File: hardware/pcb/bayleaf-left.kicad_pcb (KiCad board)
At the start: 2 copper layers, 134.9 x 92.3 mm, 70 parts, among them SW1 PG1316S, SW10 PG1316S, SW11 PG1316S, SW12 PG1316S, SW13 PG1316S, SW14 PG1316S, SW15 PG1316S, SW16 PG1316S, SW17 PG1316S, SW18 PG1316S, SW19 PG1316S, SW2 PG1316S, SW20 PG1316S, SW21 PG1316S, SW22 PG1316S, SW23 PG1316S, SW24 PG1316S, SW25 PG1316S, SW26 PG1316S, SW27 PG1316S, SW28 PG1316S, SW29 PG1316S, SW3 PG1316S, SW30 PG1316S, SW31 KMR211NGLFS, SW4 PG1316S, SW5 PG1316S, SW6 PG1316S, SW7 PG1316S, SW8 PG1316S, SW9 PG1316S, U1 nice!nano v2

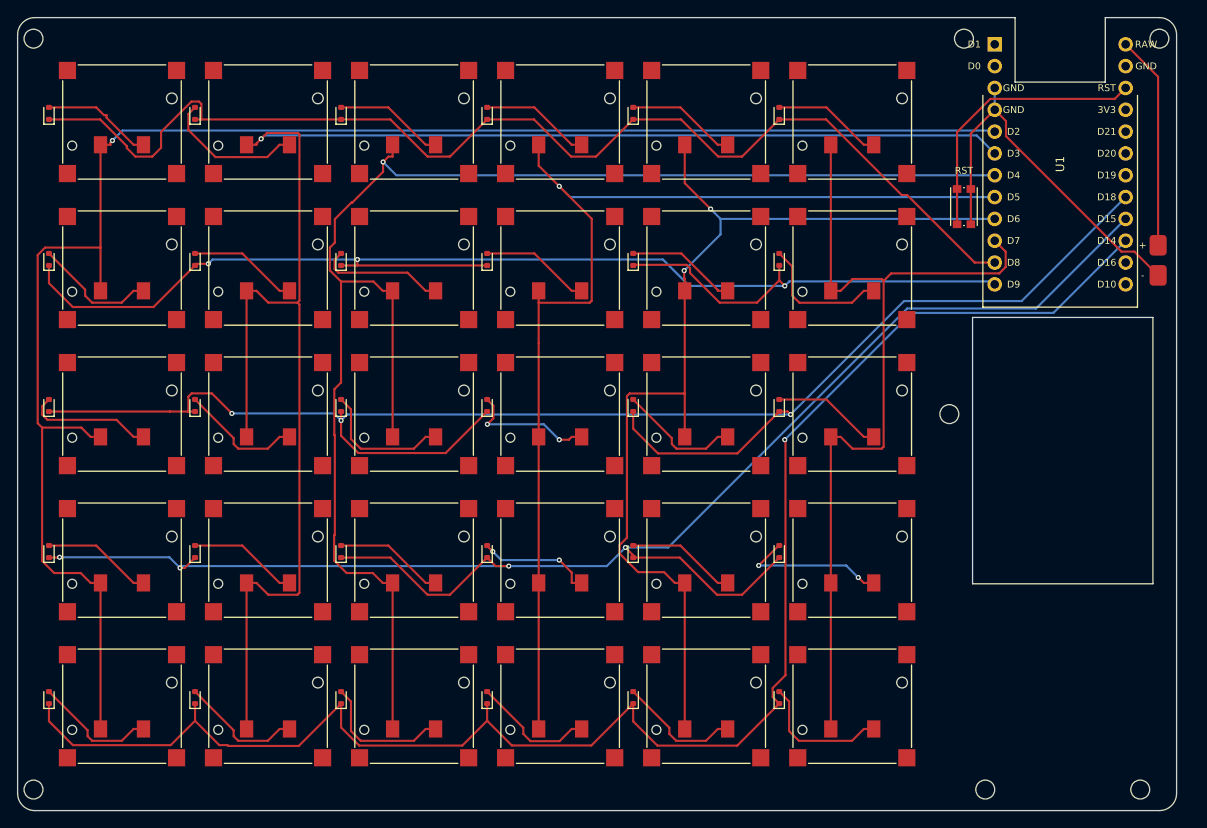
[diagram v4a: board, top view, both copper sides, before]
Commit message: Hand-solderable switches, FR4 bottom plate, reset button on the underside
- PCB: new Kailh_PG1316S_castellated footprint (window under each switch, contacts on plated
  half-holes, soldered from below with an iron; frame anchors on a small hotplate), after
  Mike Holscher's mikecinq, drawn from the Kailh land pattern. Order with castellated holes.
  Routing gets notched keepouts so Freerouting can reach the half-hole pads.
- Reset (KMR2) moves to the bottom side; the pin-hole in the plateau is gone.
- Bottom plate is now a copper-free 0.8 mm FR4 board (generate_pcb.py PlateBuilder, gerbers
  in fab/plate-*) so the radio isn't boxed in by aluminium; windows for the switch solder,
  nice!nano pins, reset button and USB-C.
- Renders (new underside view), BOM, ordering, assembly, case and schematic docs updated.

Co-Authored-By: Claude Opus 5.5 <noreply@anthropic.com>
Claude-Session: https://claude.ai/code/session_01C1HRLCKaYQawWFomwAvAgT
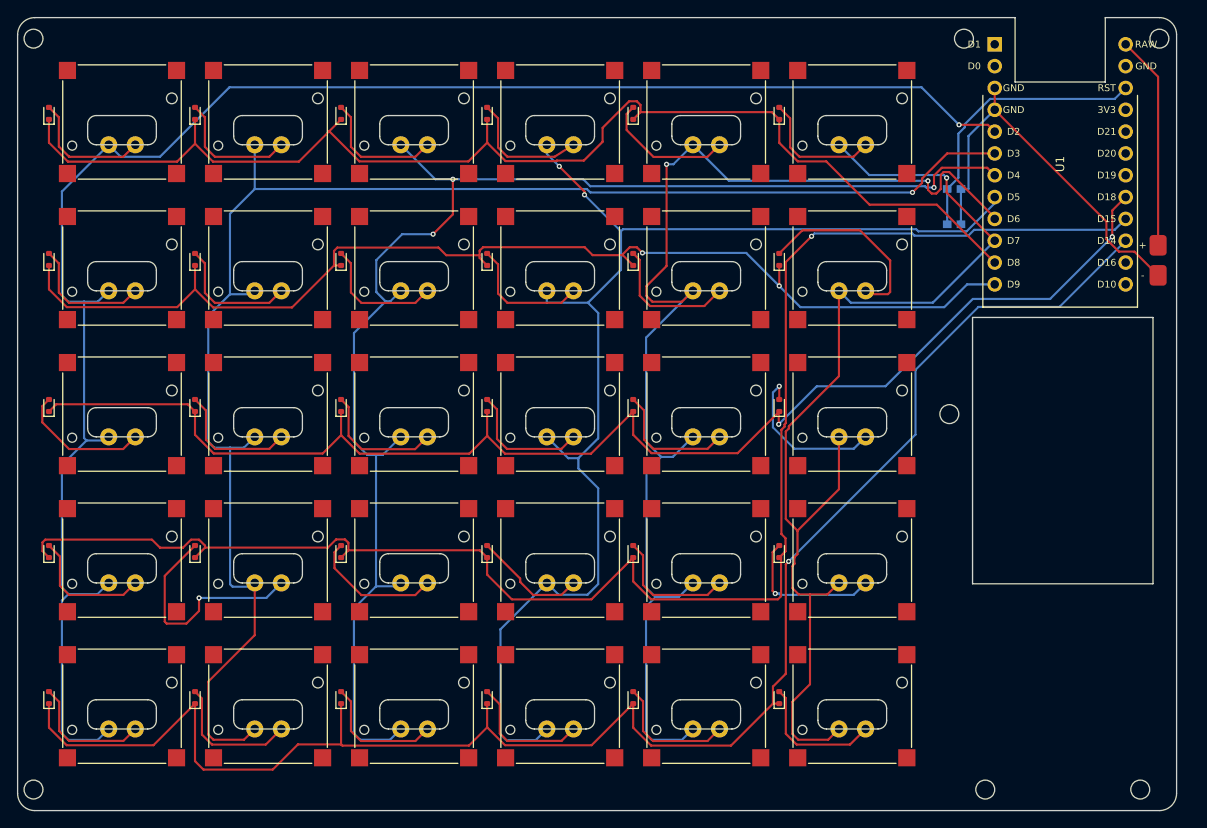
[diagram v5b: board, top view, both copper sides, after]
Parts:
- SW1, SW10, SW11, SW12, SW13, SW14, SW15, SW16, SW17, SW18, SW19, SW2, SW20, SW21, SW22, SW23, SW24, SW25, SW26, SW27, SW28, SW29, SW3, SW30, SW4, SW5, SW6, SW7, SW8, SW9: footprint bayleaf:Kailh_PG1316S -> bayleaf:Kailh_PG1316S_castellated
- SW31: moved to B.Cu
- moved SW31 1.15 mm to (109.0, 22.0), turned to -90 degrees
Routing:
- net ROW2: track 186.4 -> 160.7 mm, vias 3 -> 2
- net COL5: track 102.4 -> 125.9 mm, vias 0 -> 1
- net ROW1: track 157.8 -> 134.5 mm, vias 3 -> 2
- net COL4: track 120.9 -> 141.1 mm
- net COL3: track 129.2 -> 148.5 mm, vias 1 -> 2
- net COL1: track 194.2 -> 179.7 mm
- net N_SW20: track 12.8 -> 26.8 mm, vias 0 -> 1
- net COL2: track 172.9 -> 163.7 mm, vias 1 -> 3
- net ROW0: track 136.0 -> 142.5 mm
- net N_SW12: track 15.9 -> 22.3 mm
- net N_SW18: track 12.8 -> 19.0 mm, vias 0 -> 1
- net ROW3: track 190.6 -> 184.6 mm, vias 4 -> 1
- net COL0: track 197.6 -> 201.7 mm
- net N_SW11: track 12.9 -> 15.8 mm
- net N_SW21: track 12.8 -> 15.7 mm
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
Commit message: Switch frame anchors solderable from below: plated holes in the anchor pads
- Kailh_PG1316S_castellated: each 2x2 mm frame-anchor pad gets a 0.7 mm plated hole with a
  1.4 mm pad on the bottom, so the whole switch can be soldered from the underside with an
  iron (hotplate still works). Switch window narrowed to 7.2 mm to keep routing channels.
- Bottom plates: 2.6 mm windows under every anchor hole; silkscreen moved under the battery.
- Router: plain notches again (the 0.3 mm margin choked Freerouting); every attempt is now
  rejected if it leaves copper on a window edge.
- Docs: iron-only switch procedure (untested, try one switch first), hotplate optional.

Co-Authored-By: Claude Opus 5.5 <noreply@anthropic.com>
Claude-Session: https://claude.ai/code/session_01C1HRLCKaYQawWFomwAvAgT
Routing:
- net COL5: track 125.9 -> 105.3 mm
- net COL0: track 201.7 -> 186.1 mm
- net ROW3: track 184.6 -> 172.0 mm
- net COL1: track 179.7 -> 167.9 mm, vias 1 -> 0
- net COL3: track 148.5 -> 138.5 mm, vias 2 -> 3
- net COL2: track 163.7 -> 156.0 mm, vias 3 -> 0
- net GND: track 46.4 -> 53.9 mm
- net COL4: track 141.1 -> 134.1 mm, vias 2 -> 4
- net ROW2: track 160.7 -> 165.9 mm, vias 2 -> 1
- net N_SW20: track 26.8 -> 22.0 mm
- net N_SW6: track 15.0 -> 19.3 mm
- net ROW0: track 142.5 -> 138.3 mm
- net ROW4: track 192.4 -> 188.8 mm
- net N_SW18: track 19.0 -> 16.0 mm
- net N_SW12: track 22.3 -> 19.3 mm
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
